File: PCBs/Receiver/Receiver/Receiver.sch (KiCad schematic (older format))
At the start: 12 parts, among them P1 Digital, P2 Digital, P3 Analog, P4 Analog, U1 NRF24L01_Breakout

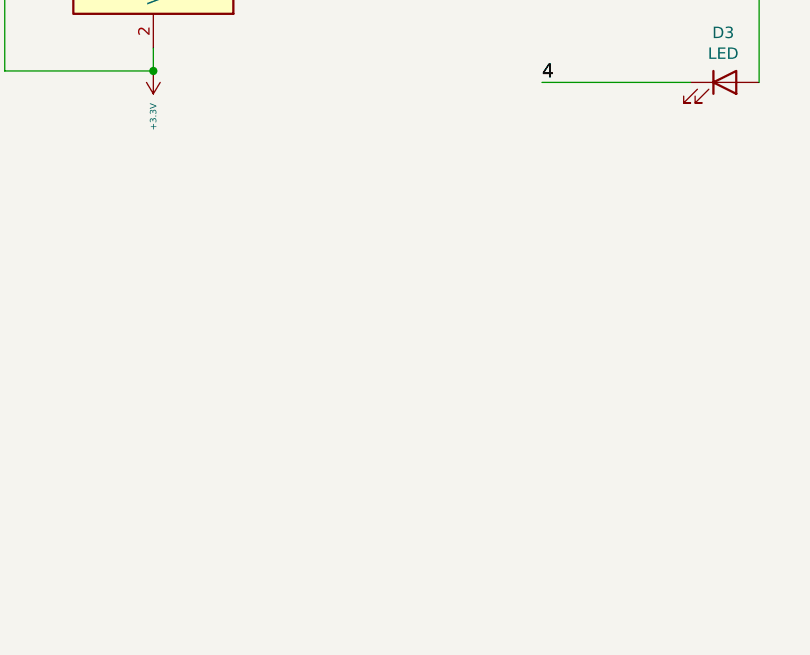
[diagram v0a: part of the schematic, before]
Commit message: added lcd sample code and schematic
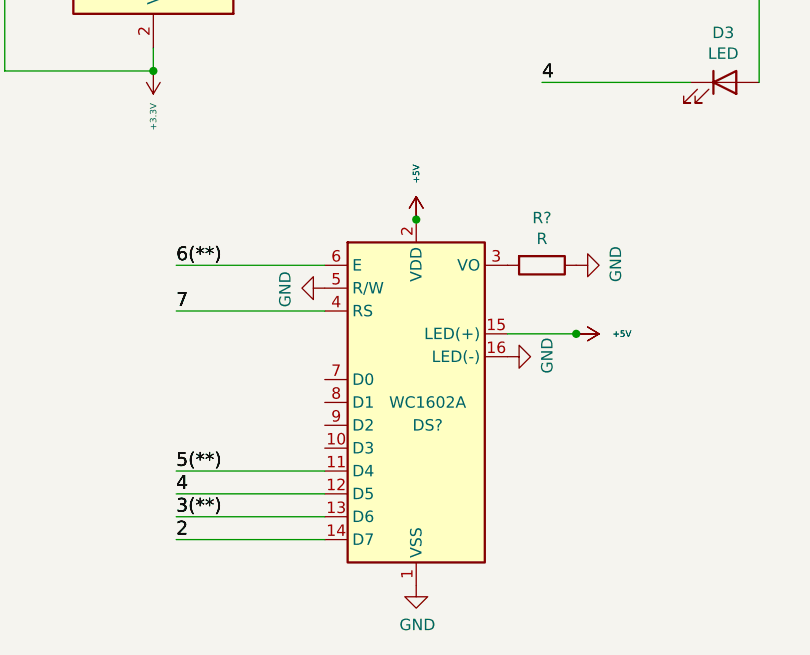
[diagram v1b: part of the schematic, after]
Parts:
- added DS?: WC1602A, Display:WC1602A, symbol Display_Character:WC1602A
- added R?: R, Resistor_THT:R_Axial_DIN0207_L6.3mm_D2.5mm_P7.62mm_Horizontal, symbol Device:R
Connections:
- net +5V: now also DS?.15 (LED(+)), DS?.2 (VDD)
- net 2: now also DS?.14 (D7)
- net 3(**): now also DS?.13 (D6)
- net 4: now also DS?.12 (D5)
- net 5(**): now also DS?.11 (D4)
- net 6(**): now also DS?.6 (E)
- net 7: now also DS?.4 (RS)
- net GND: now also DS?.1 (VSS), DS?.16 (LED(-)), DS?.5 (R/W), R?.1
- new net: DS?.3 (VO), R?.2
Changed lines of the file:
@@
 	6250 4050 6250 3400
 Connection ~ 6250 3400
+$Comp
+L Display_Character:WC1602A DS?
+U 1 1 60EADF53
+P 4750 5450
+F 0 "DS?" H 4800 5350 50  0000 C CNN
+F 1 "WC1602A" H 4800 5450 50  0000 C CNN
+F 2 "Display:WC1602A" H 4750 4550 50  0001 C CIN
+F 3 "http://www.wincomlcd.com/pdf/WC1602A-SFYLYHTC06.pdf" H 5450 5450 50  0001 C CNN
+	1    4750 5450
+	1    0    0    -1
+$EndComp
+$Comp
+L power:GND #PWR?
+U 1 1 60EAEC01
+P 4750 6250
+F 0 "#PWR?" H 4750 6000 50  0001 C CNN
+F 1 "GND" H 4755 6077 50  0000 C CNN
+F 2 "" H 4750 6250 50  0001 C CNN
+F 3 "" H 4750 6250 50  0001 C CNN
+	1    4750 6250
+	1    0    0    -1
+$EndComp
+$Comp
+L power:+5V #PWR?
+U 1 1 60EB2F42
+P 4750 4650
+F 0 "#PWR?" H 4750 4500 50  0001 C CNN
+F 1 "+5V" V 4750 4850 28  0000 C CNN
+F 2 "" H 4750 4650 50  0000 C CNN
+F 3 "" H 4750 4650 50  0000 C CNN
+	1    4750 4650
+	1    0    0    -1
+$EndComp
+$Comp
+L power:+5V #PWR?
+U 1 1 60EB2F49
+P 4750 4650
+F 0 "#PWR?" H 4750 4500 50  0001 C CNN
+F 1 "+5V" V 4750 4850 28  0000 C CNN
+F 2 "" H 4750 4650 50  0000 C CNN
+F 3 "" H 4750 4650 50  0000 C CNN
+	1    4750 4650
+	1    0    0    -1
+$EndComp
+Connection ~ 4750 4650
+$Comp
+L power:GND #PWR?
+U 1 1 60EB7B3E
+P 5450 4850
+F 0 "#PWR?" H 5450 4600 50  0001 C CNN
+F 1 "GND" H 5455 4677 50  0000 C CNN
+F 2 "" H 5450 4850 50  0001 C CNN
+F 3 "" H 5450 4850 50  0001 C CNN
+	1    5450 4850
+	0    -1   -1   0
+$EndComp
+$Comp
+L Device:R R?
+U 1 1 60EB9286
+P 5300 4850
+F 0 "R?" V 5093 4850 50  0000 C CNN
+F 1 "R" V 5184 4850 50  0000 C CNN
+F 2 "Resistor_THT:R_Axial_DIN0207_L6.3mm_D2.5mm_P7.62mm_Horizontal" V 5230 4850 50  0001 C CNN
+F 3 "~" H 5300 4850 50  0001 C CNN
+	1    5300 4850
+	0    1    1    0
+$EndComp
+Text Label 3700 5050 0    60   ~ 0
+7
+Wire Wire Line
+	4350 5050 3700 5050
+Text Label 3700 5050 0    60   ~ 0
+7
+$Comp
+L power:GND #PWR?
+U 1 1 60EBC2D4
+P 4350 4950
+F 0 "#PWR?" H 4350 4700 50  0001 C CNN
+F 1 "GND" H 4355 4777 50  0000 C CNN
+F 2 "" H 4350 4950 50  0001 C CNN
+F 3 "" H 4350 4950 50  0001 C CNN
+	1    4350 4950
+	0    1    1    0
+$EndComp
+Text Label 3700 4850 0    60   ~ 0
+6(**)
+Wire Wire Line
+	3700 4850 4350 4850
+Text Label 3700 4850 0    60   ~ 0
+6(**)
+Text Label 3700 5750 0    60   ~ 0
+5(**)
+Wire Wire Line
+	4350 5750 3700 5750
+Text Label 3700 5750 0    60   ~ 0
+5(**)
+Text Label 3700 5850 0    60   ~ 0
+4
+Wire Wire Line
+	3700 5850 4350 5850
+Text Label 3700 5850 0    60   ~ 0
+4
+Text Label 3700 5950 0    60   ~ 0
+3(**)
+Wire Wire Line
+	4350 5950 3700 5950
+Text Label 3700 5950 0    60   ~ 0
+3(**)
+Text Label 3700 6050 0    60   ~ 0
+2
+Wire Wire Line
+	3700 6050 4350 6050
+Text Label 3700 6050 0    60   ~ 0
+2
+$Comp
+L power:GND #PWR?
+U 1 1 60EC73B7
+P 5150 5250
+F 0 "#PWR?" H 5150 5000 50  0001 C CNN
+F 1 "GND" H 5155 5077 50  0000 C CNN
+F 2 "" H 5150 5250 50  0001 C CNN
+F 3 "" H 5150 5250 50  0001 C CNN
+	1    5150 5250
+	0    -1   -1   0
+$EndComp
+$Comp
+L power:+5V #PWR?
+U 1 1 60EC9EF5
+P 5450 5150
+F 0 "#PWR?" H 5450 5000 50  0001 C CNN
+F 1 "+5V" V 5450 5350 28  0000 C CNN
+F 2 "" H 5450 5150 50  0000 C CNN
+F 3 "" H 5450 5150 50  0000 C CNN
+	1    5450 5150
+	0    1    1    0
+$EndComp
+$Comp
+L power:+5V #PWR?
+U 1 1 60EC9EFB
+P 5450 5150
+F 0 "#PWR?" H 5450 5000 50  0001 C CNN
+F 1 "+5V" V 5450 5350 28  0000 C CNN
+F 2 "" H 5450 5150 50  0000 C CNN
+F 3 "" H 5450 5150 50  0000 C CNN
+	1    5450 5150
+	0    1    1    0
+$EndComp
+Wire Wire Line
+	5450 5150 5150 5150
+Connection ~ 5450 5150
 $EndSCHEMATC

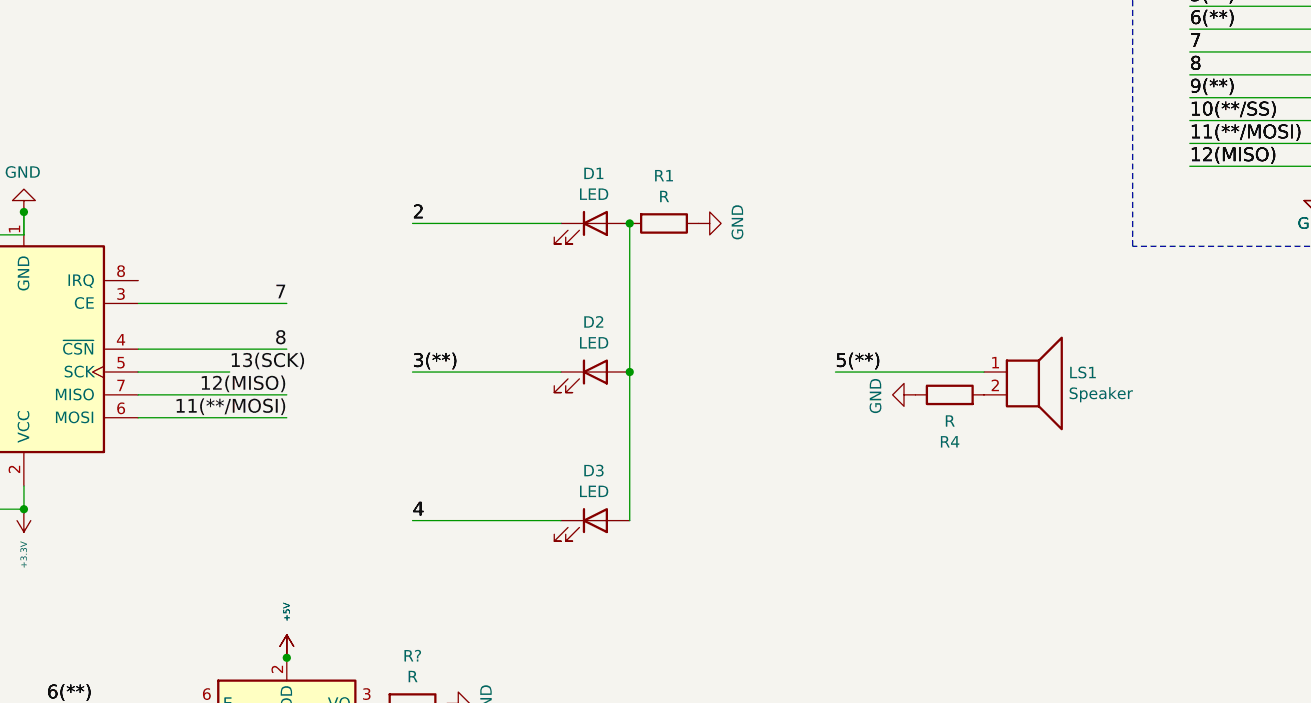
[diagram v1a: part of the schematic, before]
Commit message: updated schematic for receiver and transmitter
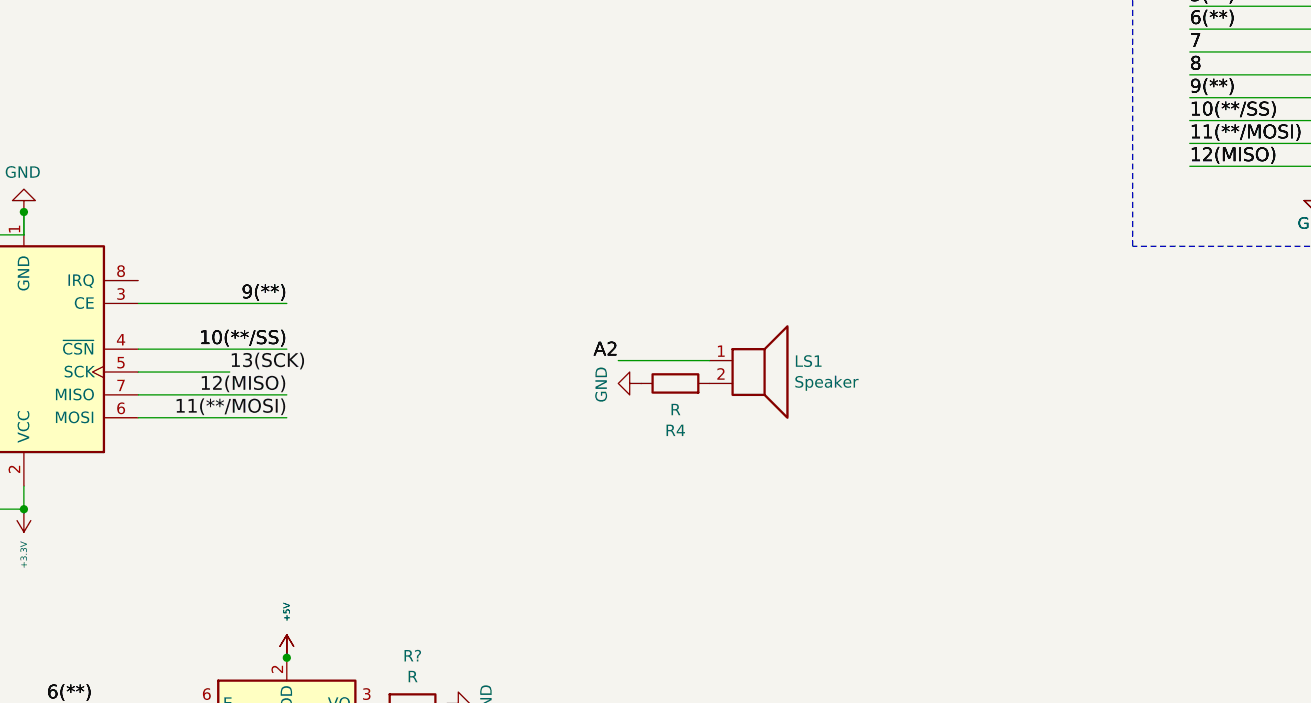
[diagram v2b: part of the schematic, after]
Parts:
- removed D1, D2, D3: LED, LED_THT:LED_D3.0mm, symbol Device:LED
- removed R1: R, Resistor_THT:R_Axial_DIN0207_L6.3mm_D2.5mm_P7.62mm_Horizontal, symbol Device:R
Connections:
- net 10(**/SS): now also U1.4 (~CSN)
- net 5(**): no longer LS1.1
- net 7: no longer U1.3 (CE)
- net 8: no longer U1.4 (~CSN)
- net 9(**): now also U1.3 (CE)
- net A2: now also LS1.1
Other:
- moved on the sheet: LS1, R4
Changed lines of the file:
@@
 13(SCK)
-Wire Wire Line
-	4750 3300 4100 3300
-Text Label 4750 3300 2    60   ~ 0
-8
-Wire Wire Line
-	4100 3100 4750 3100
-Text Label 4750 3100 2    60   ~ 0
-7
 Wire Wire Line
 	2950 4000 3600 4000
@@
 Connection ~ 3600 4000
 $Comp
-L Device:LED D2
-U 1 1 60E4D82D
-P 6100 3400
-F 0 "D2" H 6093 3617 50  0000 C CNN
-F 1 "LED" H 6093 3526 50  0000 C CNN
-F 2 "LED_THT:LED_D3.0mm" H 6100 3400 50  0001 C CNN
-F 3 "~" H 6100 3400 50  0001 C CNN
-	1    6100 3400
-	1    0    0    -1
-$EndComp
-$Comp
-L Device:LED D3
-U 1 1 60E4F5C0
-P 6100 4050
-F 0 "D3" H 6093 4267 50  0000 C CNN
-F 1 "LED" H 6093 4176 50  0000 C CNN
-F 2 "LED_THT:LED_D3.0mm" H 6100 4050 50  0001 C CNN
-F 3 "~" H 6100 4050 50  0001 C CNN
-	1    6100 4050
-	1    0    0    -1
-$EndComp
-Text Label 5300 2750 0    60   ~ 0
-2
-Wire Wire Line
-	5300 2750 5950 2750
-Text Label 5300 2750 0    60   ~ 0
-2
-Text Label 5300 3400 0    60   ~ 0
-3(**)
-Wire Wire Line
-	5950 3400 5300 3400
-Text Label 5300 3400 0    60   ~ 0
-3(**)
-Text Label 5300 4050 0    60   ~ 0
-4
-Wire Wire Line
-	5300 4050 5950 4050
-Text Label 5300 4050 0    60   ~ 0
-4
-$Comp
-L Device:LED D1
-U 1 1 60E4CED8
-P 6100 2750
-F 0 "D1" H 6093 2967 50  0000 C CNN
-F 1 "LED" H 6093 2876 50  0000 C CNN
-F 2 "LED_THT:LED_D3.0mm" H 6100 2750 50  0001 C CNN
-F 3 "~" H 6100 2750 50  0001 C CNN
-	1    6100 2750
-	1    0    0    -1
-$EndComp
-$Comp
 L Device:Speaker LS1
 U 1 1 60E5AC0D
-P 8000 3400
-F 0 "LS1" H 8170 3396 50  0000 L CNN
-F 1 "Speaker" H 8170 3305 50  0000 L CNN
-F 2 "Resistor_THT:R_Axial_DIN0207_L6.3mm_D2.5mm_P7.62mm_Horizontal" H 8000 3200 50  0001 C CNN
-F 3 "~" H 7990 3350 50  0001 C CNN
-	1    8000 3400
-	1    0    0    -1
-$EndComp
-Text Label 7150 3400 0    60   ~ 0
-5(**)
-Wire Wire Line
-	7800 3400 7150 3400
-Text Label 7150 3400 0    60   ~ 0
-5(**)
-$Comp
-L power:GND #PWR03
-U 1 1 60E72C85
-P 6550 2750
-F 0 "#PWR03" H 6550 2500 50  0001 C CNN
-F 1 "GND" H 6555 2577 50  0000 C CNN
-F 2 "" H 6550 2750 50  0001 C CNN
-F 3 "" H 6550 2750 50  0001 C CNN
-	1    6550 2750
-	0    -1   -1   0
-$EndComp
-$Comp
-L Device:R R1
-U 1 1 60E72C8B
-P 6400 2750
-F 0 "R1" V 6193 2750 50  0000 C CNN
-F 1 "R" V 6284 2750 50  0000 C CNN
-F 2 "Resistor_THT:R_Axial_DIN0207_L6.3mm_D2.5mm_P7.62mm_Horizontal" V 6330 2750 50  0001 C CNN
-F 3 "~" H 6400 2750 50  0001 C CNN
-	1    6400 2750
-	0    1    1    0
+P 6800 3350
+F 0 "LS1" H 6970 3346 50  0000 L CNN
+F 1 "Speaker" H 6970 3255 50  0000 L CNN
+F 2 "Resistor_THT:R_Axial_DIN0207_L6.3mm_D2.5mm_P7.62mm_Horizontal" H 6800 3150 50  0001 C CNN
+F 3 "~" H 6790 3300 50  0001 C CNN
+	1    6800 3350
+	1    0    0    -1
 $EndComp
 $Comp
 L power:GND #PWR06
 U 1 1 60E74D34
-P 7500 3500
-F 0 "#PWR06" H 7500 3250 50  0001 C CNN
-F 1 "GND" H 7505 3327 50  0000 C CNN
-F 2 "" H 7500 3500 50  0001 C CNN
-F 3 "" H 7500 3500 50  0001 C CNN
-	1    7500 3500
+P 6300 3450
+F 0 "#PWR06" H 6300 3200 50  0001 C CNN
+F 1 "GND" H 6305 3277 50  0000 C CNN
+F 2 "" H 6300 3450 50  0001 C CNN
+F 3 "" H 6300 3450 50  0001 C CNN
+	1    6300 3450
 	0    1    1    0
 $EndComp
@@
 L Device:R R4
 U 1 1 60E74D3A
-P 7650 3500
-F 0 "R4" V 7443 3500 50  0000 C CNN
-F 1 "R" V 7534 3500 50  0000 C CNN
-F 2 "Resistor_THT:R_Axial_DIN0207_L6.3mm_D2.5mm_P7.62mm_Horizontal" V 7580 3500 50  0001 C CNN
-F 3 "~" H 7650 3500 50  0001 C CNN
-	1    7650 3500
+P 6450 3450
+F 0 "R4" V 6243 3450 50  0000 C CNN
+F 1 "R" V 6334 3450 50  0000 C CNN
+F 2 "Resistor_THT:R_Axial_DIN0207_L6.3mm_D2.5mm_P7.62mm_Horizontal" V 6380 3450 50  0001 C CNN
+F 3 "~" H 6450 3450 50  0001 C CNN
+	1    6450 3450
 	0    -1   -1   0
 $EndComp
-Wire Wire Line
-	6250 3400 6250 2750
-Connection ~ 6250 2750
-Wire Wire Line
-	6250 4050 6250 3400
-Connection ~ 6250 3400
 $Comp
 L Display_Character:WC1602A DS?
@@
 	5450 5150 5150 5150
 Connection ~ 5450 5150
+Text Label 4750 3100 2    60   ~ 0
+9(**)
+Wire Wire Line
+	4100 3100 4750 3100
+Text Label 4750 3100 2    60   ~ 0
+9(**)
+Text Label 4750 3300 2    60   ~ 0
+10(**/SS)
+Wire Wire Line
+	4750 3300 4100 3300
+Text Label 4750 3300 2    60   ~ 0
+10(**/SS)
+Text Label 6200 3350 2    60   ~ 0
+A2
+Wire Wire Line
+	6200 3350 6600 3350
+Text Label 6200 3350 2    60   ~ 0
+A2
 $EndSCHEMATC

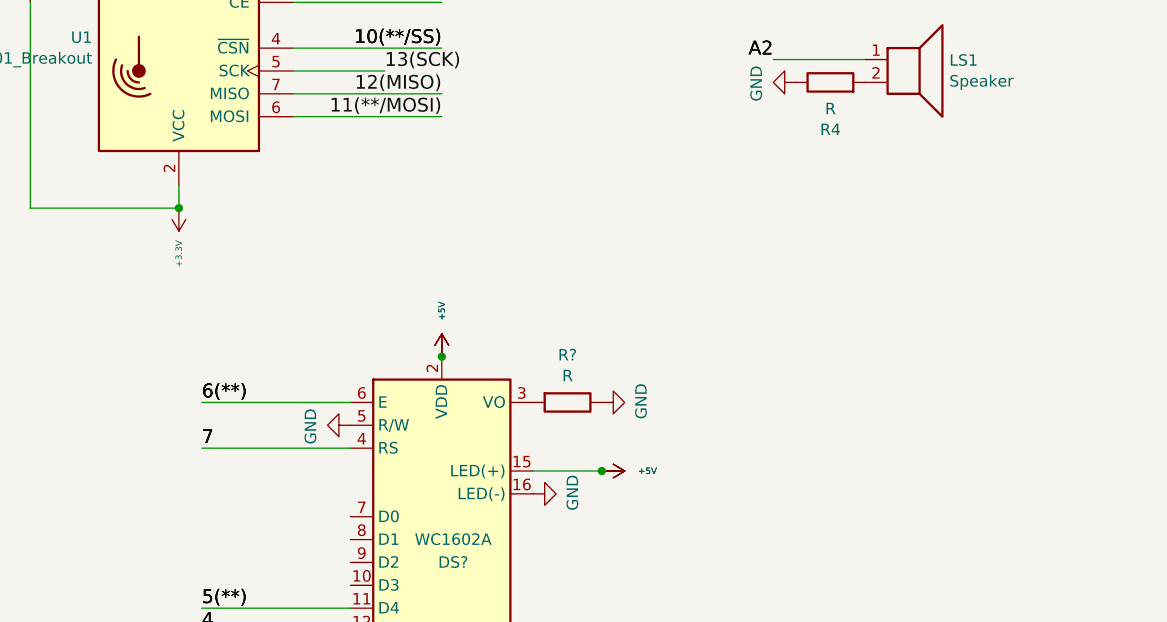
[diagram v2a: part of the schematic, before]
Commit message: added test files for receiver and transmitter
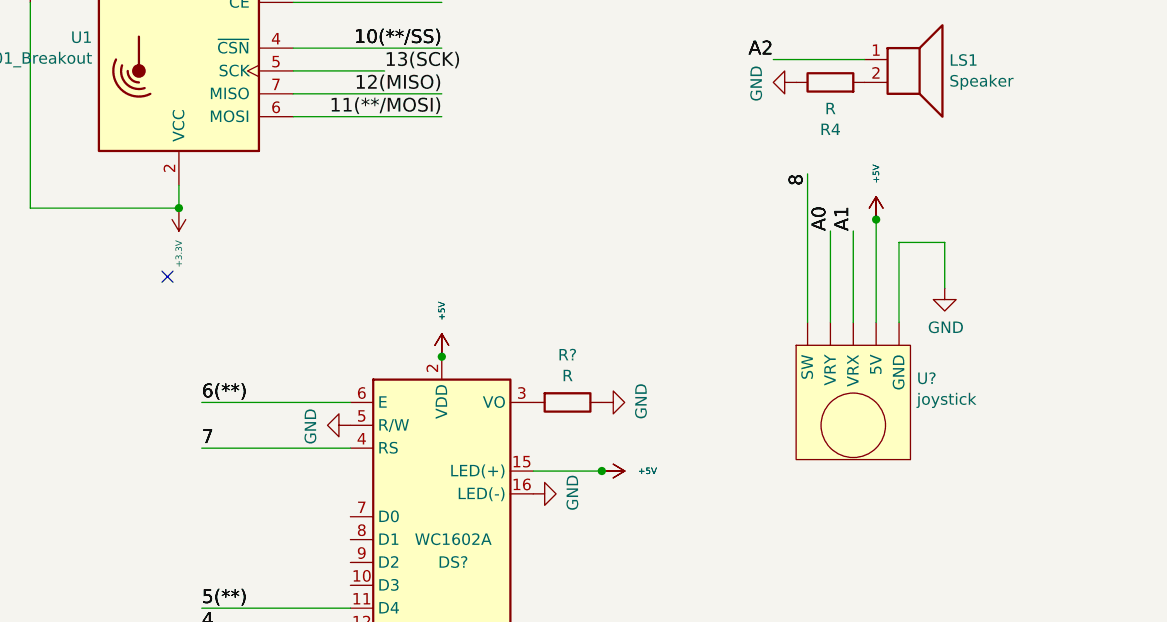
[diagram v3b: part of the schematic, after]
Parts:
- added U?: joystick, symbol alvin:joystick
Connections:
- net +5V: now also U?.~ (VRY)
- net 8: now also U?.~ (VRY)
- net A0: now also U?.~ (VRY)
- net A1: now also U?.~ (VRY)
- net GND: now also U?.~ (VRY)
- no-connect marks 0 -> 1
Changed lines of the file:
@@
 Text Label 6200 3350 2    60   ~ 0
 A2
+$Comp
+L alvin:joystick U?
+U 1 1 60EEFA48
+P 6550 4550
+F 0 "U?" H 6828 4354 50  0000 L CNN
+F 1 "joystick" H 6828 4263 50  0000 L CNN
+F 2 "" H 6700 4650 50  0001 C CNN
+F 3 "" H 6700 4650 50  0001 C CNN
+	1    6550 4550
+	1    0    0    -1
+$EndComp
+Text Label 6450 4100 1    60   ~ 0
+A0
+Wire Wire Line
+	6450 4100 6450 4500
+Text Label 6450 4100 1    60   ~ 0
+A0
+Text Label 6550 4100 1    60   ~ 0
+A1
+Wire Wire Line
+	6550 4500 6550 4100
+Text Label 6550 4100 1    60   ~ 0
+A1
+$Comp
+L power:+5V #PWR?
+U 1 1 60EF7360
+P 6650 4050
+F 0 "#PWR?" H 6650 3900 50  0001 C CNN
+F 1 "+5V" V 6650 4250 28  0000 C CNN
+F 2 "" H 6650 4050 50  0000 C CNN
+F 3 "" H 6650 4050 50  0000 C CNN
+	1    6650 4050
+	1    0    0    -1
+$EndComp
+Wire Wire Line
+	6650 4050 6650 4500
+$Comp
+L power:+5V #PWR?
+U 1 1 60EF7367
+P 6650 4050
+F 0 "#PWR?" H 6650 3900 50  0001 C CNN
+F 1 "+5V" V 6650 4250 28  0000 C CNN
+F 2 "" H 6650 4050 50  0000 C CNN
+F 3 "" H 6650 4050 50  0000 C CNN
+	1    6650 4050
+	1    0    0    -1
+$EndComp
+Connection ~ 6650 4050
+Text Label 6350 3850 3    60   ~ 0
+8
+Wire Wire Line
+	6350 3850 6350 4500
+Text Label 6350 3850 3    60   ~ 0
+8
+$Comp
+L power:GND #PWR?
+U 1 1 60EFC592
+P 6950 4350
+F 0 "#PWR?" H 6950 4100 50  0001 C CNN
+F 1 "GND" H 6955 4177 50  0000 C CNN
+F 2 "" H 6950 4350 50  0001 C CNN
+F 3 "" H 6950 4350 50  0001 C CNN
+	1    6950 4350
+	1    0    0    -1
+$EndComp
+Wire Wire Line
+	6750 4500 6750 4150
+Wire Wire Line
+	6750 4150 6950 4150
+Wire Wire Line
+	6950 4150 6950 4350
+NoConn ~ 3550 4300
 $EndSCHEMATC

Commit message: edited schematic
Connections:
- no-connect marks 1 -> 0
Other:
- moved on the sheet: C1, DS?, LS1, R4, R?, U1, U?
